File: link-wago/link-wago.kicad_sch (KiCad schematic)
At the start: 29 parts, among them J101 2x05_Horizontal, J102 NE8FAH, J103 DX07S016JA3, J104 2x05_Horizontal, J105 NE8FAH, J106 WAGO 2601-1101, J107 WAGO 2065-100, J108 WAGO 2065-100, J109 WAGO 2601-1101, J110 WAGO 2065-100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

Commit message: Use date as revision
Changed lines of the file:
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@@
 	(title_block
 		(title "V2 Link WAGO")
-		(date "2026-01-12")
-		(rev "3")
+		(date "2026-02-10")
+		(rev "2026-01-12")
 		(company "Versio Duo")
 		(comment 1 "External Power Supply")
@@
 	(symbol
 		(lib_id "V2_power:PWR_FLAG")
-		(at 227.33 29.21 90)
+		(at 227.33 29.21 0)
 		(unit 1)
 		(exclude_from_sim no)
@@
 		(dnp no)
 		(property "Reference" "#FLG0102"
-			(at 225.425 29.21 0)
+			(at 227.33 27.305 0)
 			(effects
 				(font
@@
 		)
 		(property "Value" "PWR_FLAG"
-			(at 217.932 29.21 90)
+			(at 218.186 29.21 0)
 			(effects
 				(font
@@
 		)
 		(property "Description" "Special symbol for telling ERC where power comes from"
-			(at 244.602 29.21 0)
+			(at 227.33 46.482 0)
 			(effects
 				(font
@@
 	(symbol
 		(lib_id "V2_power:PWR_FLAG")
-		(at 227.33 34.29 90)
+		(at 227.33 34.29 0)
 		(unit 1)
 		(exclude_from_sim no)
@@
 		(dnp no)
 		(property "Reference" "#FLG0103"
-			(at 225.425 34.29 0)
+			(at 227.33 32.385 0)
 			(effects
 				(font
@@
 		)
 		(property "Value" "PWR_FLAG"
-			(at 217.932 34.29 90)
+			(at 218.186 34.29 0)
 			(effects
 				(font
@@
 		)
 		(property "Description" "Special symbol for telling ERC where power comes from"
-			(at 244.602 34.29 0)
+			(at 227.33 51.562 0)
 			(effects
 				(font
@@
 	(symbol
 		(lib_id "V2_power:PWR_FLAG")
-		(at 227.33 39.37 90)
+		(at 227.33 39.37 0)
 		(unit 1)
 		(exclude_from_sim no)
@@
 		(dnp no)
 		(property "Reference" "#FLG0104"
-			(at 225.425 39.37 0)
+			(at 227.33 37.465 0)
 			(effects
 				(font
@@
 		)
 		(property "Value" "PWR_FLAG"
-			(at 217.932 39.37 90)
+			(at 217.932 39.37 0)
 			(effects
 				(font
@@
 		)
 		(property "Description" "Special symbol for telling ERC where power comes from"
-			(at 244.602 39.37 0)
+			(at 227.33 56.642 0)
 			(effects
 				(font
@@
 	)
 	(embedded_fonts no)
+	(embedded_files
+		(file
+			(name "V2_A4.kicad_wks")
+			(type worksheet)
+			(data |KLUv/WBhBk0QALbYTiEQtRsmZc5q276ayLS71D6kxbkmoTeIJM7lAHtEAMAAxQFGAD8ARQCbvIHa
+				a/wrVHSazXnPhvzar1BNtH1kxRf5EwCAQPh5F+e0kJq0nmtfKDvj37Jf3xQUlFKqztoXWzE7iAAI
+				iJ6Q5m2d9RAC9jcPPWe/GXf/9ewpPR3+uPbv7bdzvr37wXlr2X8dBHFXu7Z3HUG7Kvrz9qKU7eB2
+				v/MM4n/Mhfg5G5sn7WsDTS2mA1WyssZDsy4YdpEGzfD8Ny+85JzH7H+961FjX/x0qtq0MdaqJ8dx
+				k1KAwF+soV3VFnEoqewX+XNfTaqqPatRlLsbgcKhzs5+29sEzSaWRPZ4txDEjpmZNCoSiiMhaUwy
+				y4Jg3oe5pmhPRSS7MtJAerbfnYNNgaEkuCg6oVzYhbEsF1vRgtxS55zTIVig4URjFFJTI1qYFNIB
+				YESmRusYYvaiF0uSUdhu1Q2lFiOgdmN7VvaH2oWyw9MQXRuZtQQQoIsxFn2ldtnpQiUNa0HvDQCK
+				f/XTisCgEJQEXe/if4EJsakkqj8BMmGAU+ZM/AG8LSEJMfgkOKfSKPhw4rD3ZHfmNZYNfDMigEPJ
+				EBoIDghtm1kJ8BAQ8xyGdkOuFQy33sishFt8DZNX4uNRXJZ5hBy746RJaNtgbfyB613d0dov6Cdg
+				iUQT9BXkf9EiYDuODpB6gKkC|
+			)
+			(checksum "0A61268C685EAF945CA2EA8187370BD3")
+		)
+	)
 )

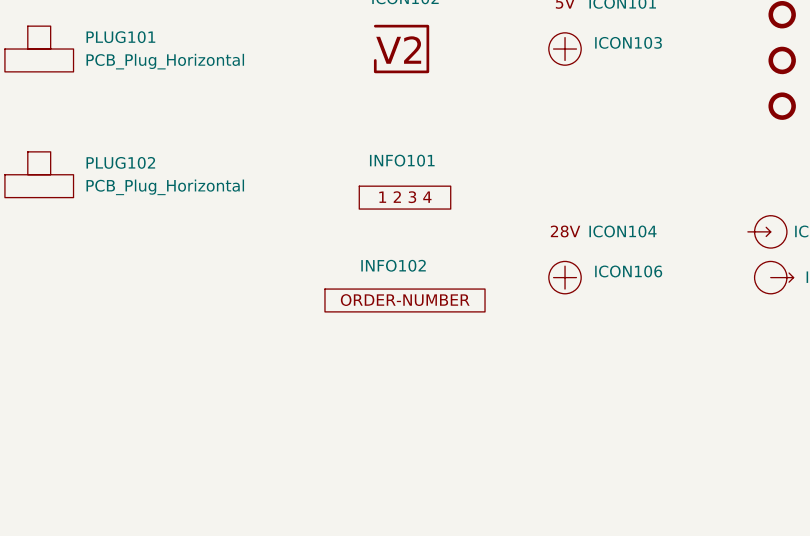
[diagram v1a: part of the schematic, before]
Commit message: Replace Order_Number
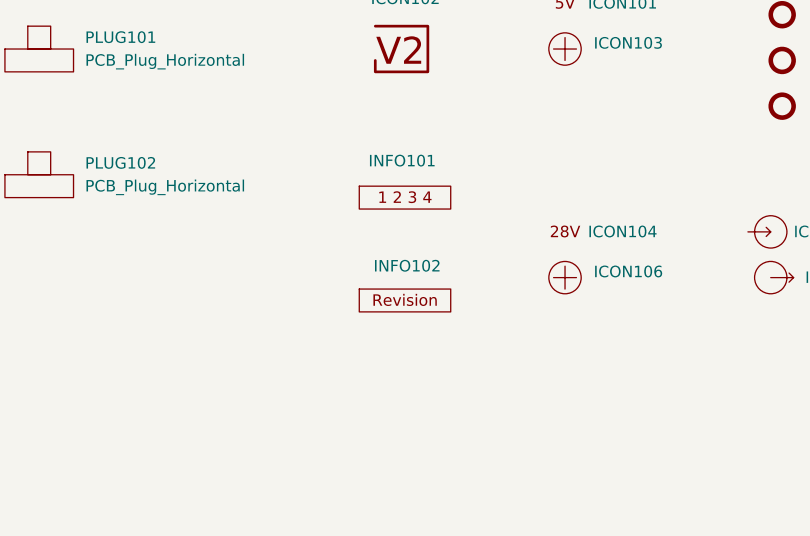
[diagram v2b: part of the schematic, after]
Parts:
- INFO102: value Order_Number -> (none); footprint V2_Production:Order_Number -> V2_Production:Revision; symbol V2_Production:Order_Number -> V2_Production:Revision
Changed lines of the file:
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@@
 		(at 187.96 162.56 0)
 		(unit 1)
-		(exclude_from_sim no)
+		(exclude_from_sim yes)
 		(in_bom no)
 		(on_board yes)
@@
 			)
 		)
-		(property "Sim.Enable" "0"
-			(at 187.96 162.56 0)
-			(effects
-				(font
-					(size 1.27 1.27)
-				)
-				(hide yes)
-			)
-		)
 		(instances
 			(project "power-rj45"
@@
 		(at 187.96 148.59 0)
 		(unit 1)
-		(exclude_from_sim no)
+		(exclude_from_sim yes)
 		(in_bom no)
 		(on_board yes)
@@
 			)
 		)
-		(property "Sim.Enable" "0"
-			(at 187.96 148.59 0)
-			(effects
-				(font
-					(size 1.27 1.27)
-				)
-				(hide yes)
-			)
-		)
 		(instances
 			(project "power-rj45"
@@
 		(at 246.38 148.59 0)
 		(unit 1)
-		(exclude_from_sim no)
+		(exclude_from_sim yes)
 		(in_bom no)
 		(on_board yes)
@@
 			)
 		)
-		(property "Sim.Enable" "0"
-			(at 246.38 148.59 0)
-			(effects
-				(font
-					(size 1.27 1.27)
-				)
-				(hide yes)
-			)
-		)
 		(instances
 			(project "power-rj45"
@@
 		(at 269.24 173.99 0)
 		(unit 1)
-		(exclude_from_sim no)
+		(exclude_from_sim yes)
 		(in_bom no)
 		(on_board yes)
@@
 			)
 		)
-		(property "Sim.Enable" "0"
-			(at 269.24 173.99 0)
-			(effects
-				(font
-					(size 1.27 1.27)
-				)
-				(hide yes)
-			)
-		)
 		(instances
 			(project ""
@@
 	)
 	(symbol
-		(lib_id "V2_Production:Order_Number")
+		(lib_id "V2_Production:Revision")
 		(at 228.6 176.53 0)
 		(unit 1)
@@
 		(dnp no)
 		(property "Reference" "INFO102"
-			(at 227.33 172.72 0)
+			(at 228.854 172.72 0)
 			(effects
 				(font
@@
 			)
 		)
-		(property "Value" "Order_Number"
+		(property "Value" ""
 			(at 228.6 179.07 0)
 			(effects
@@
 			)
 		)
-		(property "Footprint" "V2_Production:Order_Number"
+		(property "Footprint" "V2_Production:Revision"
 			(at 228.6 181.61 0)
 			(effects
@@
 		(at 246.38 143.51 0)
 		(unit 1)
-		(exclude_from_sim no)
+		(exclude_from_sim yes)
 		(in_bom no)
 		(on_board yes)
@@
 			)
 		)
-		(property "Sim.Enable" "0"
-			(at 246.38 143.51 0)
-			(effects
-				(font
-					(size 1.27 1.27)
-				)
-				(hide yes)
-			)
-		)
 		(instances
 			(project "power-rj45"
@@
 		(at 246.38 173.99 0)
 		(unit 1)
-		(exclude_from_sim no)
+		(exclude_from_sim yes)
 		(in_bom no)
 		(on_board yes)
@@
 			)
 		)
-		(property "Sim.Enable" "0"
-			(at 246.38 173.99 0)
-			(effects
-				(font
-					(size 1.27 1.27)
-				)
-				(hide yes)
-			)
-		)
 		(instances
 			(project "power-rj45"
@@
 		(at 269.24 168.91 0)
 		(unit 1)
-		(exclude_from_sim no)
+		(exclude_from_sim yes)
 		(in_bom no)
 		(on_board yes)
@@
 			)
 		)
-		(property "Sim.Enable" "0"
-			(at 269.24 168.91 0)
-			(effects
-				(font
-					(size 1.27 1.27)
-				)
-				(hide yes)
-			)
-		)
 		(instances
 			(project ""
@@
 		(at 228.6 148.59 0)
 		(unit 1)
-		(exclude_from_sim no)
+		(exclude_from_sim yes)
 		(in_bom no)
 		(on_board yes)
@@
 			(at 228.6 148.59 0)
 			(effects
-				(font
-					(size 1.27 1.27)
-				)
-				(hide yes)
-			)
-		)
-		(property "Sim.Enable" "0"
-			(at 228.6 148.59 0)
-			(effects

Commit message: Update Library
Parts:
- C101: symbol V2_Device:C_0603_0u1 -> V2_Capacitor:0603_0u1
- R101, R102: symbol V2_Device:R_0603_5k1 -> V2_Resistor:0603_5k1
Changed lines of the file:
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@@
 	)
 	(symbol
-		(lib_id "V2_Device:C_0603_0u1")
+		(lib_id "V2_Capacitor:0603_0u1")
 		(at 95.25 157.48 0)
 		(unit 1)
@@
 	)
 	(symbol
-		(lib_id "V2_Device:R_0603_5k1")
+		(lib_id "V2_Resistor:0603_5k1")
 		(at 252.73 63.5 90)
 		(unit 1)
@@
 	)
 	(symbol
-		(lib_id "V2_Device:R_0603_5k1")
+		(lib_id "V2_Resistor:0603_5k1")
 		(at 252.73 66.04 90)
 		(unit 1)

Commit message: Refresh
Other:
- note added: "PoE Passive +28V IEEE 802.3af Mode B"
- note removed: "PoE Passive +24V IEEE 802.3af Mode B"
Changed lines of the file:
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@@
 		(comment 1 "External Power Supply")
 	)
-	(text "PoE Passive +24V\nIEEE 802.3af Mode B"
+	(text "PoE Passive +28V\nIEEE 802.3af Mode B"
 		(exclude_from_sim no)
 		(at 46.736 115.57 0)

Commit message: Export stencil
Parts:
- INFO102: value (none) -> ~

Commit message: Replace step-down
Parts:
- ICON104, INFO102: value ~ -> (none)

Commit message: Update
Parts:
- C101: Id (none) -> Capacitor:${SYMBOL_NAME}
- J101: renamed from J106; Id (none) -> WAGO:${SYMBOL_NAME}; Rating (none) -> 17.5A
- J102: renamed from J109; Id (none) -> WAGO:${SYMBOL_NAME}; Rating (none) -> 17.5A
- J103: renamed from J102; Id (none) -> EtherCon:${SYMBOL_NAME}; Rating (none) -> CAT5e
- J104: renamed from J105; Id (none) -> EtherCon:${SYMBOL_NAME}; Rating (none) -> CAT5e
- J105: renamed from J101; Id (none) -> Header:${SYMBOL_NAME}; Rating (none) -> 1A
- J106: renamed from J104; Id (none) -> Header:${SYMBOL_NAME}; Rating (none) -> 1A
- J107: Id (none) -> WAGO:${SYMBOL_NAME}; Rating (none) -> 9A
- J108: renamed from J110; Id (none) -> WAGO:${SYMBOL_NAME}; Rating (none) -> 9A
- J109: renamed from J108; Id (none) -> WAGO:${SYMBOL_NAME}; Rating (none) -> 9A
- J110: renamed from J111; Id (none) -> WAGO:${SYMBOL_NAME}; Rating (none) -> 9A
- J111: renamed from J103; Id (none) -> USB:${SYMBOL_NAME}; Rating (none) -> USB2.0
- R101, R102: Id (none) -> Resistor:${SYMBOL_NAME}
- TVS101: Id (none) -> Diode:${SYMBOL_NAME}
- renumbered ICON102 to ICON101, ICON101 to ICON102, ICON106 to ICON105, ICON105 to ICON106

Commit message: Good Bye Imperial
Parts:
- C101: footprint V2_Capacitor_SMD:C_0603 -> V2_Capacitor_SMD:C_1608; symbol V2_Capacitor:0603_0u1 -> V2_Capacitor:1608_0u1
- R101, R102: footprint V2_Resistor_SMD:R_0603 -> V2_Resistor_SMD:R_1608; symbol V2_Resistor:0603_5k1 -> V2_Resistor:1608_5k1
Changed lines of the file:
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@@
 	)
 	(symbol
-		(lib_id "V2_Capacitor:0603_0u1")
+		(lib_id "V2_Capacitor:1608_0u1")
 		(at 95.25 157.48 0)
 		(unit 1)
@@
 			)
 		)
-		(property "Footprint" "V2_Capacitor_SMD:C_0603"
+		(property "Footprint" "V2_Capacitor_SMD:C_1608"
 			(at 95.25 174.498 0)
 			(hide yes)
@@
 	)
 	(symbol
-		(lib_id "V2_Resistor:0603_5k1")
+		(lib_id "V2_Resistor:1608_5k1")
 		(at 252.73 63.5 90)
 		(unit 1)
@@
 			)
 		)
-		(property "Footprint" "V2_Resistor_SMD:R_0603"
+		(property "Footprint" "V2_Resistor_SMD:R_1608"
 			(at 268.478 63.5 0)
 			(hide yes)
@@
 	)
 	(symbol
-		(lib_id "V2_Resistor:0603_5k1")
+		(lib_id "V2_Resistor:1608_5k1")
 		(at 252.73 66.04 90)
 		(unit 1)
@@
 			)
 		)
-		(property "Footprint" "V2_Resistor_SMD:R_0603"
+		(property "Footprint" "V2_Resistor_SMD:R_1608"
 			(at 268.478 66.04 0)
 			(hide yes)
